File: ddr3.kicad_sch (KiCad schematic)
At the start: 26 parts, among them U11 LIFCL-40-9BG256C, U12 MT41K128M16JT-125_K

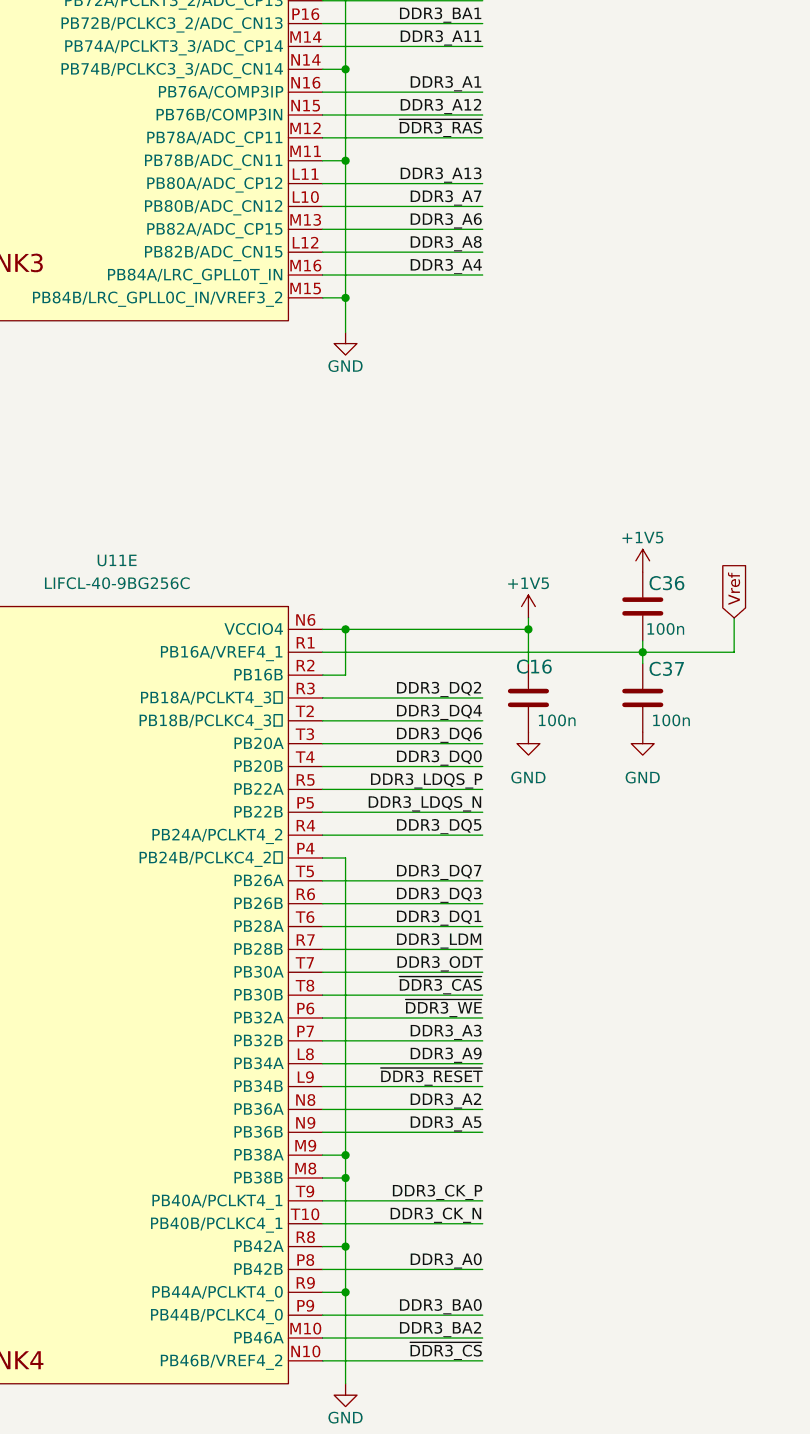
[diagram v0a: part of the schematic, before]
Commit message: Rerouted some DDR3 signals
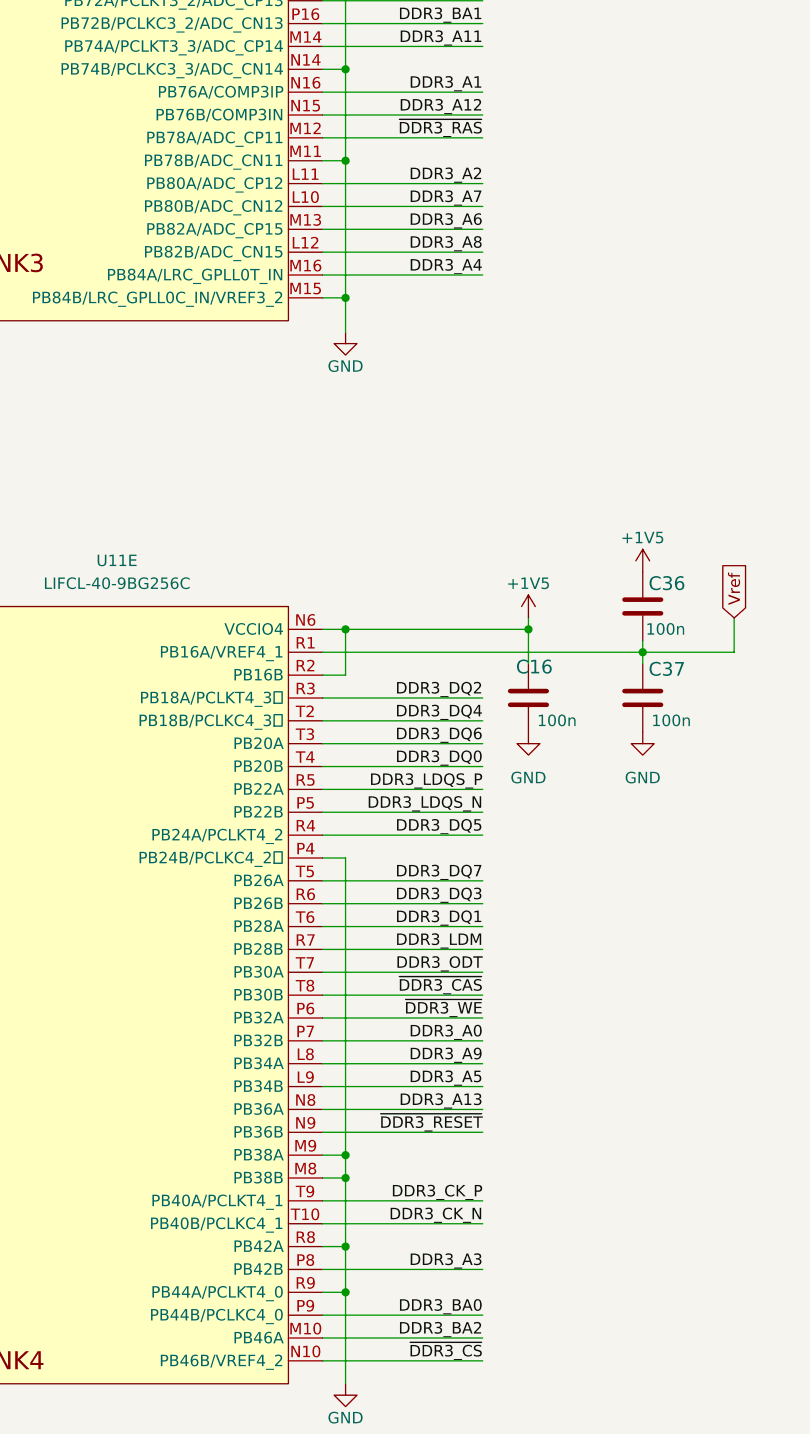
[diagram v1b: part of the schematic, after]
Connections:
- net DDR3_A0: now also U11.P7 (PB32B); no longer U11.P8 (PB42B)
- net DDR3_A13: now also U11.N8 (PB36A); no longer U11.L11 (PB80A/ADC_CP12)
- net DDR3_A2: now also U11.L11 (PB80A/ADC_CP12); no longer U11.N8 (PB36A)
- net DDR3_A3: now also U11.P8 (PB42B); no longer U11.P7 (PB32B)
- net DDR3_A5: now also U11.L9 (PB34B); no longer U11.N9 (PB36B)
- net ~{DDR3_RESET}: now also U11.N9 (PB36B); no longer U11.L9 (PB34B)
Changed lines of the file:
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@@
     (effects (font (size 1.27 1.27)) (justify left bottom))
   )
-  (label "DDR3_A3" (at 113.03 219.71 180)
+  (label "DDR3_A3" (at 113.03 245.11 180)
     (effects (font (size 1.27 1.27)) (justify right bottom))
   )
@@
     (effects (font (size 1.27 1.27)) (justify left bottom))
   )
-  (label "DDR3_A2" (at 113.03 227.33 180)
+  (label "DDR3_A2" (at 113.03 124.46 180)
     (effects (font (size 1.27 1.27)) (justify right bottom))
   )
@@
     (effects (font (size 1.27 1.27)) (justify left bottom))
   )
-  (label "DDR3_A13" (at 113.03 124.46 180)
+  (label "DDR3_A13" (at 113.03 227.33 180)
     (effects (font (size 1.27 1.27)) (justify right bottom))
   )
@@
     (effects (font (size 1.27 1.27)) (justify right bottom))
   )
-  (label "DDR3_A0" (at 113.03 245.11 180)
-    (effects (font (size 1.27 1.27)) (justify right bottom))
-  )
-  (label "~{DDR3_RESET}" (at 113.03 224.79 180)
+  (label "DDR3_A0" (at 113.03 219.71 180)
+    (effects (font (size 1.27 1.27)) (justify right bottom))
+  )
+  (label "~{DDR3_RESET}" (at 113.03 229.87 180)
     (effects (font (size 1.27 1.27)) (justify right bottom))
   )
@@
     (effects (font (size 1.27 1.27)) (justify right bottom))
   )
-  (label "DDR3_A5" (at 113.03 229.87 180)
-    (effects (font (size 1.27 1.27)) (justify right bottom))
-  )
+  (label "DDR3_A5" (at 113.03 224.79 180)
+    (effects (font (size 1.27 1.27)) (justify right bottom))
+  )

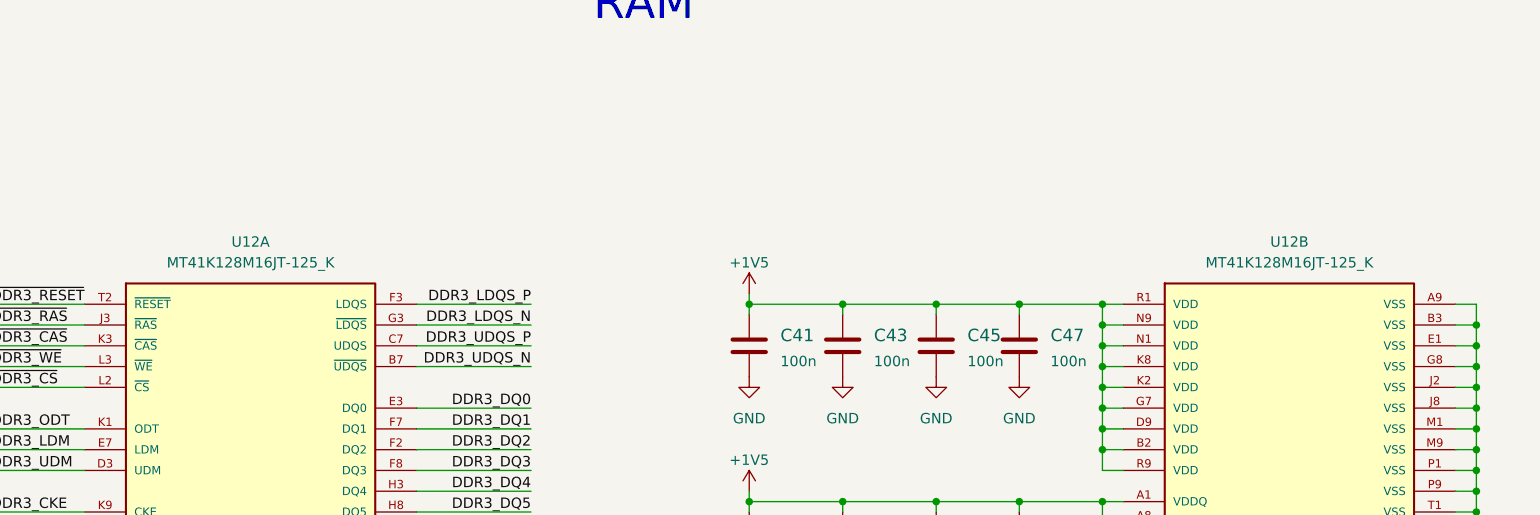
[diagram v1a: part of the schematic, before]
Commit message: Added QWIIC connector
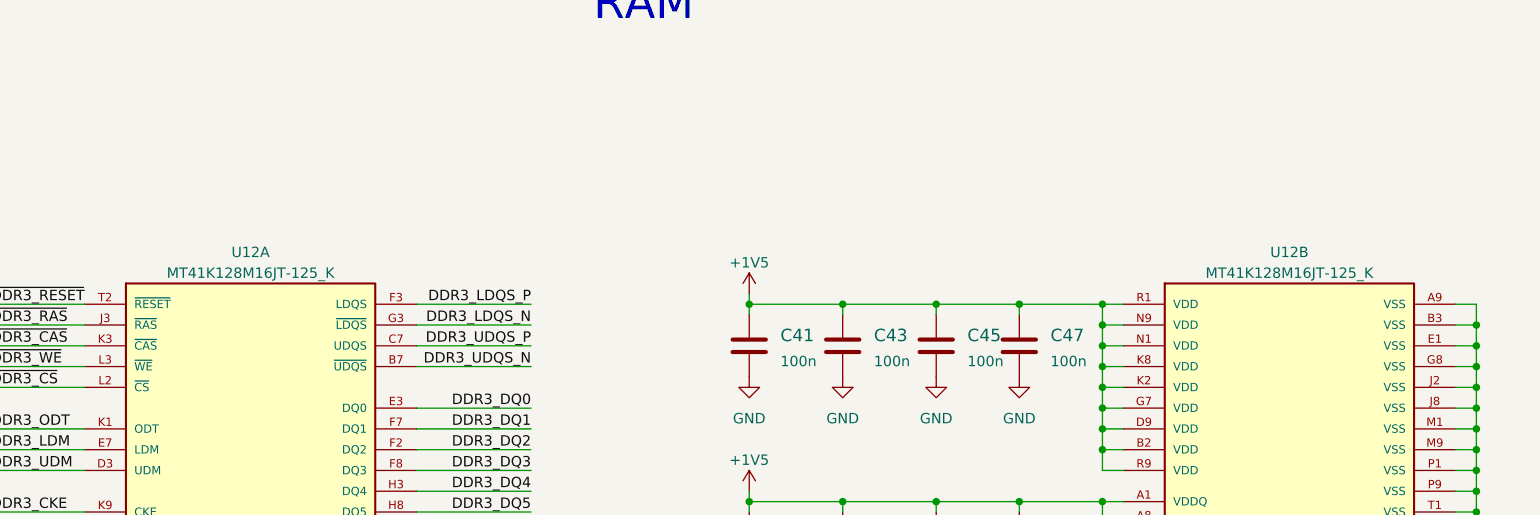
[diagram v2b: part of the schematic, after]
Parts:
- removed U12: MT41K128M16JT-125_K, crosslink-nx-video-converter-footprints:BGA80P96C6X16_800X1400X110, symbol crosslink-nx-video-converter:MT41K128M16JT-125_K
- added U12: MT41K128M16JT-125_K, antmicro-footprints:BGA80P96C6X16_800X1400X110, symbol antmicroMemory:MT41K128M16JT-125_K
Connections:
- net +1V5: now also U12.A1 (VDDQ), U12.A8 (VDDQ), U12.B2 (VDD), U12.C1 (VDDQ), U12.C9 (VDDQ), U12.D2 (VDDQ), U12.D9 (VDD), U12.E9 (VDDQ), U12.F1 (VDDQ), U12.G7 (VDD), U12.H2 (VDDQ), U12.H9 (VDDQ), U12.K2 (VDD), U12.K8 (VDD), U12.N1 (VDD), U12.N9 (VDD), U12.R1 (VDD), U12.R9 (VDD)
- net DDR3_A0: now also U12.N3 (A0)
- net DDR3_A1: now also U12.P7 (A1)
- net DDR3_A10: now also U12.L7 (A10/AP)
- net DDR3_A11: now also U12.R7 (A11)
- net DDR3_A12: now also U12.N7 (A12/!BC)
- net DDR3_A13: now also U12.T3 (A13)
- net DDR3_A2: now also U12.P3 (A2)
- net DDR3_A3: now also U12.N2 (A3)
- net DDR3_A4: now also U12.P8 (A4)
- net DDR3_A5: now also U12.P2 (A5)
- net DDR3_A6: now also U12.R8 (A6)
- net DDR3_A7: now also U12.R2 (A7)
- net DDR3_A8: now also U12.T8 (A8)
- net DDR3_A9: now also U12.R3 (A9)
- net DDR3_BA0: now also U12.M2 (BA0)
- net DDR3_BA1: now also U12.N8 (BA1)
- net DDR3_BA2: now also U12.M3 (BA2)
- net DDR3_CKE: now also U12.K9 (CKE)
- net DDR3_CK_N: now also U12.K7 (~{CK})
- net DDR3_CK_P: now also U12.J7 (CK)
- net DDR3_DQ0: now also U12.E3 (DQ0)
- net DDR3_DQ1: now also U12.F7 (DQ1)
- net DDR3_DQ10: now also U12.C8 (DQ10)
- net DDR3_DQ11: now also U12.C2 (DQ11)
- net DDR3_DQ12: now also U12.A7 (DQ12)
- net DDR3_DQ13: now also U12.A2 (DQ13)
- net DDR3_DQ14: now also U12.B8 (DQ14)
- net DDR3_DQ15: now also U12.A3 (DQ15)
- net DDR3_DQ2: now also U12.F2 (DQ2)
- net DDR3_DQ3: now also U12.F8 (DQ3)
- net DDR3_DQ4: now also U12.H3 (DQ4)
- net DDR3_DQ5: now also U12.H8 (DQ5)
- net DDR3_DQ6: now also U12.G2 (DQ6)
- net DDR3_DQ7: now also U12.H7 (DQ7)
- net DDR3_DQ8: now also U12.D7 (DQ8)
- net DDR3_DQ9: now also U12.C3 (DQ9)
- net DDR3_LDM: now also U12.E7 (LDM)
- net DDR3_LDQS_N: now also U12.G3 (~{LDQS})
- net DDR3_LDQS_P: now also U12.F3 (LDQS)
- net DDR3_ODT: now also U12.K1 (ODT)
- net DDR3_UDM: now also U12.D3 (UDM)
- net DDR3_UDQS_N: now also U12.B7 (~{UDQS})
- net DDR3_UDQS_P: now also U12.C7 (UDQS)
- net GND: now also U12.A9 (VSS), U12.B1 (VSSQ), U12.B3 (VSS), U12.B9 (VSSQ), U12.D1 (VSSQ), U12.D8 (VSSQ), U12.E1 (VSS), U12.E2 (VSSQ), U12.E8 (VSSQ), U12.F9 (VSSQ), U12.G1 (VSSQ), U12.G8 (VSS), U12.G9 (VSSQ), U12.J2 (VSS), U12.J8 (VSS), U12.M1 (VSS), U12.M9 (VSS), U12.P1 (VSS), U12.P9 (VSS), U12.T1 (VSS), U12.T9 (VSS)
- net Vref: now also U12.H1 (VREFDQ), U12.M8 (VREFCA)
- net ~{DDR3_CAS}: now also U12.K3 (~{CAS})
- net ~{DDR3_CS}: now also U12.L2 (~{CS})
- net ~{DDR3_RAS}: now also U12.J3 (~{RAS})
- net ~{DDR3_RESET}: now also U12.T2 (~{RESET})
- net ~{DDR3_WE}: now also U12.L3 (~{WE})
- net at R47.2: now also U12.L8 (ZQ)
- new net: U12.J1, U12.J9, U12.L1, U12.L9, U12.M7, U12.T7

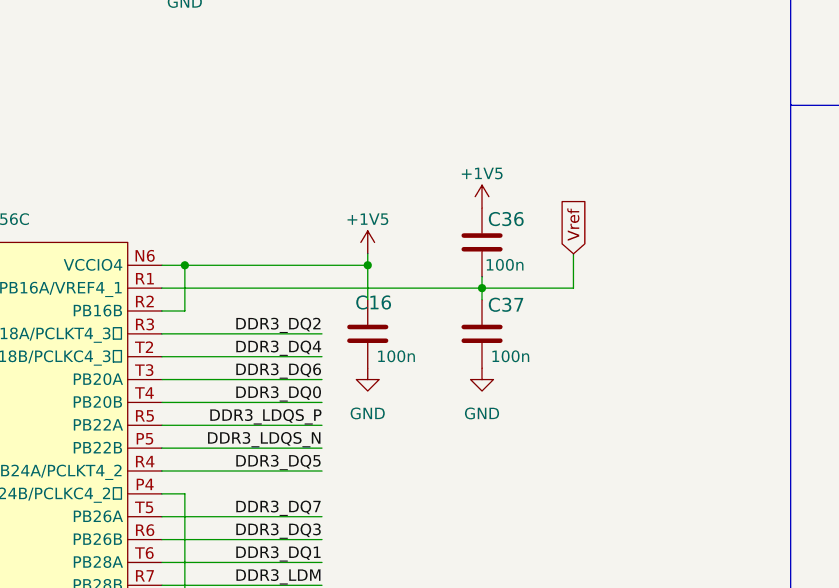
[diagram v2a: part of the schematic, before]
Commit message: Placed decoupling capacitors
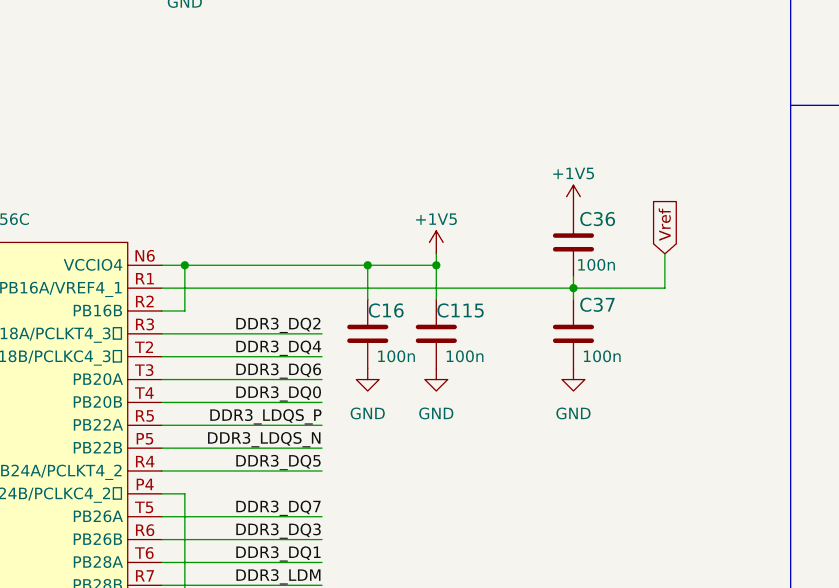
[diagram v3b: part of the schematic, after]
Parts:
- added C115: C_100n_0402, crosslink-nx-video-converter-footprints:0402-cap, symbol crosslink-nx-video-converter:C_100n_0402
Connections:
- net +1V5: now also C115.1
- net GND: now also C115.2
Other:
- moved on the sheet: C36, C37
